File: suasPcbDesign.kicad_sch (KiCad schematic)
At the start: 94 parts, among them J1 SENSE_IB, J2 SPI CS, J4 SPI CTRL, J5 PWM CTRL, J6 JTAG Pinout, J7 USB_C_Receptacle_USB2.0_16P, SW1 SW_SPST, SW2 SW_SPST, SW3 SW_SPST, SW4 SW_SPST, SW5 SW_SPST, SW6 SW_SPST, SW7 SW_SPST, U1 74HC138, U2 LMR51625DDC, U3 MCP3562RT-E/ST, U5 TLV77733PDBVR, U6 LMV331, U7 ESP32-S3-WROOM-1, U8 LM66100DCK, U9 USBLC6-2SC6

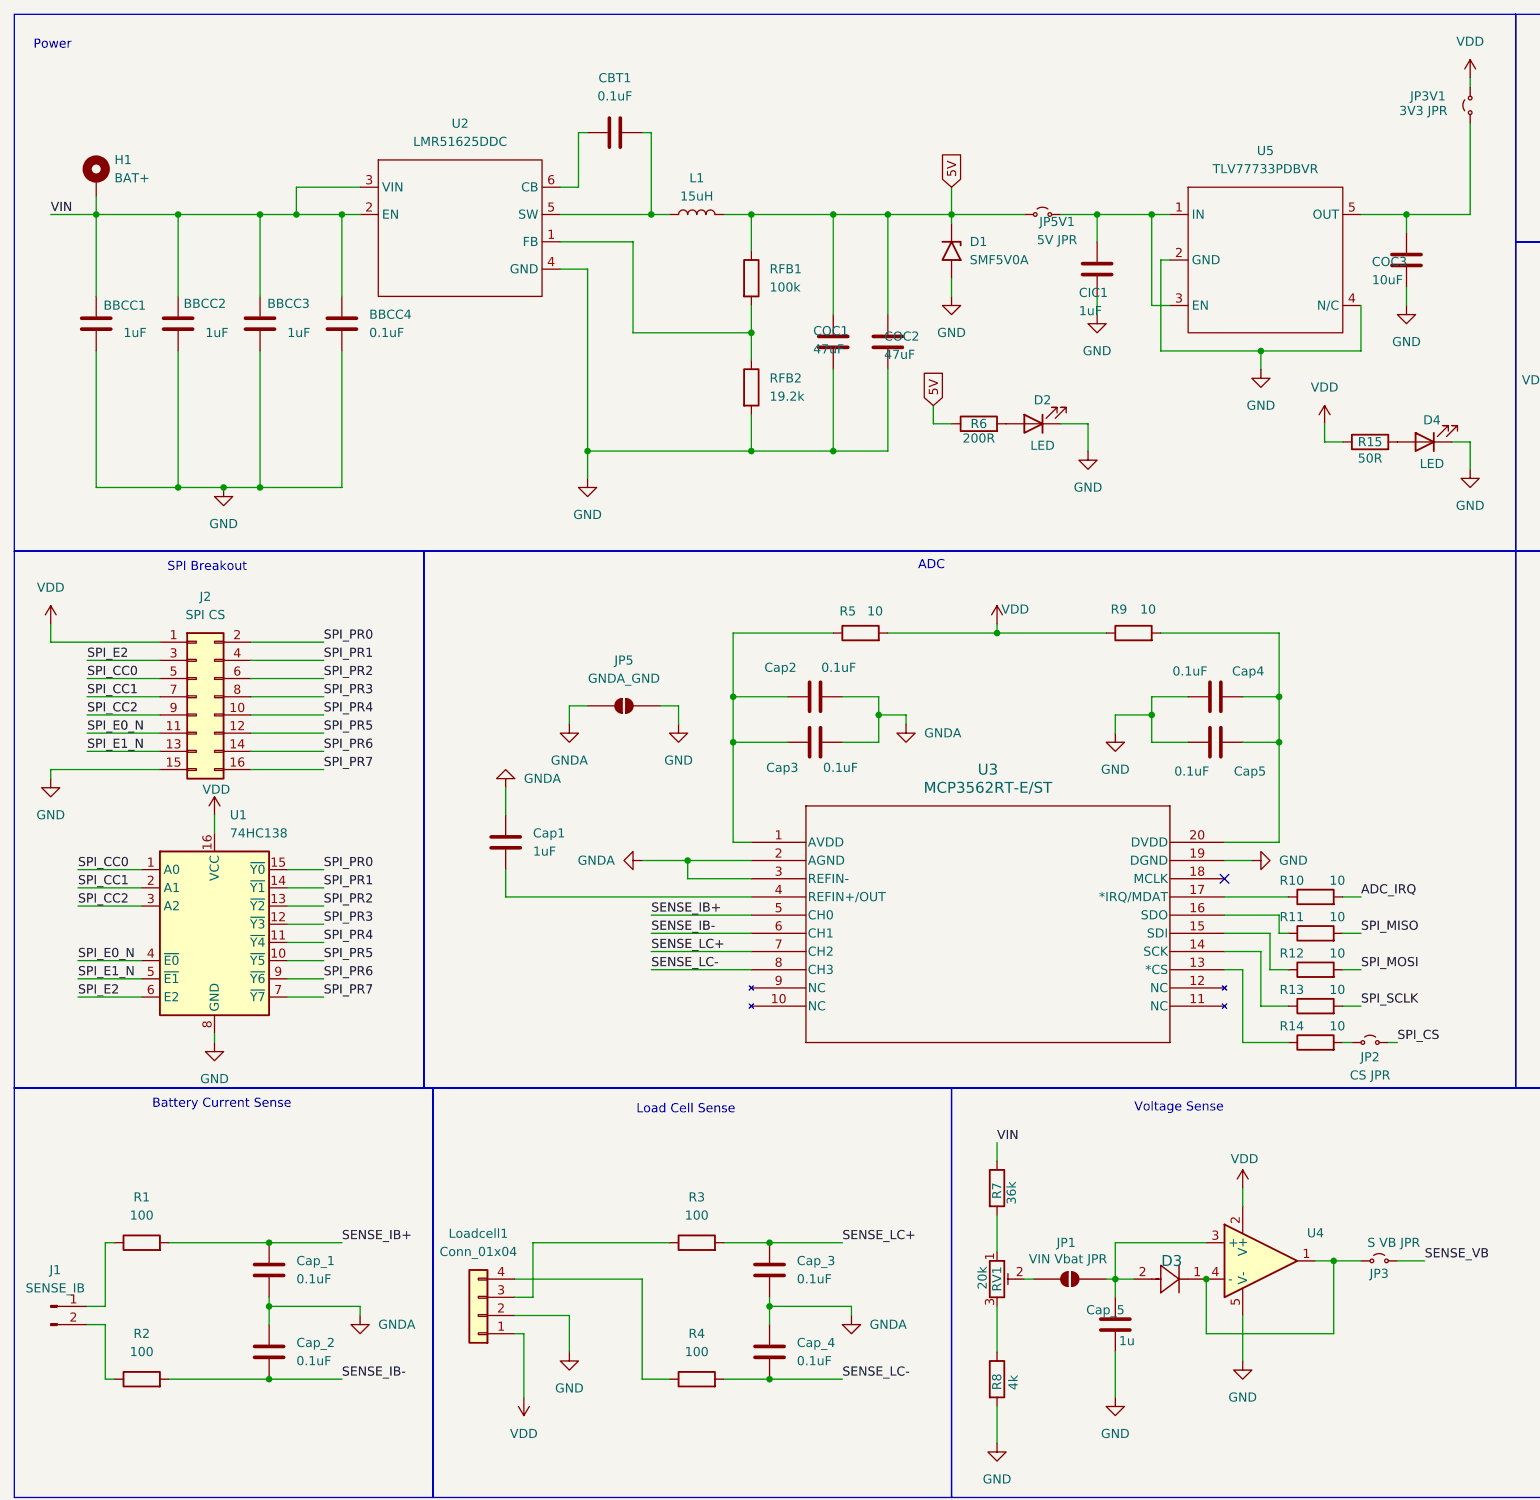
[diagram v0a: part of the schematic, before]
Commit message: Change resistor value to 100R instead of 50
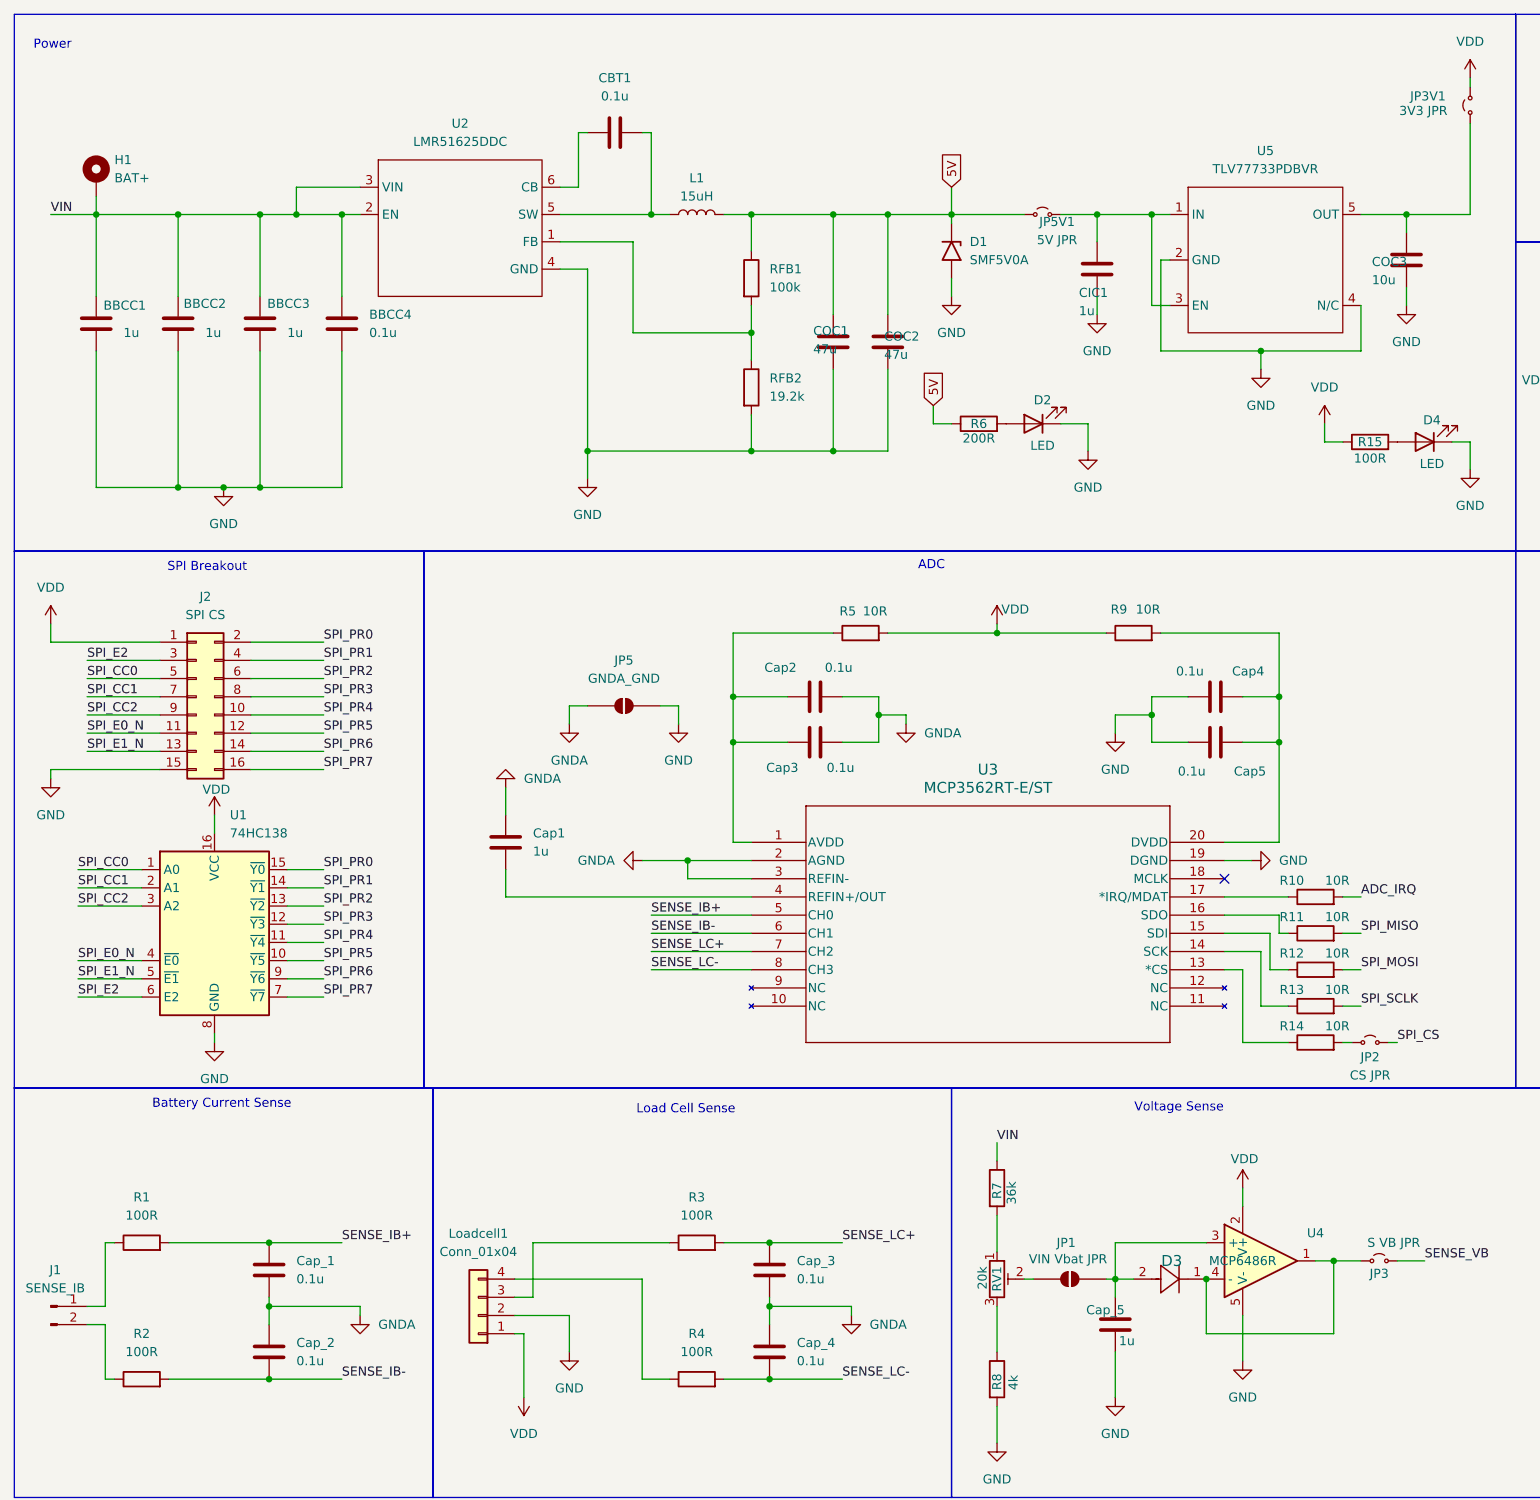
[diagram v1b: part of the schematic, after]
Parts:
- BBCC1, BBCC2, BBCC3, CIC1, Cap1: value 1uF -> 1u
- BBCC4, CBT1, Cap2, Cap3, Cap4, Cap5, Cap_1, Cap_2, Cap_3, Cap_4: value 0.1uF -> 0.1u
- COC1, COC2: value 47uF -> 47u
- COC3: value 10uF -> 10u
- R1, R2, R3, R4: value 100 -> 100R
- R10, R11, R12, R13, R14, R5, R9: value 10 -> 10R
- R15: value 50R -> 100R
- U4: value (none) -> MCP6486R
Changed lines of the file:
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@@
 			)
 		)
-		(property "Value" "47uF"
+		(property "Value" "47u"
 			(at 137.922 64.008 0)
 			(show_name no)
@@
 			)
 		)
-		(property "Value" "47uF"
+		(property "Value" "47u"
 			(at 128.016 63.246 0)
 			(show_name no)
@@
 			)
 		)
-		(property "Value" "0.1uF"
+		(property "Value" "0.1u"
 			(at 131.826 121.666 90)
 			(show_name no)
@@
 			)
 		)
-		(property "Value" "0.1uF"
+		(property "Value" "0.1u"
 			(at 180.594 108.204 90)
 			(show_name no)
@@
 			)
 		)
-		(property "Value" "1uF"
+		(property "Value" "1u"
 			(at 54.61 60.9599 0)
 			(show_name no)
@@
 			)
 		)
-		(property "Value" "50R"
+		(property "Value" "100R"
 			(at 205.74 78.486 90)
 			(show_name no)
@@
 			)
 		)
-		(property "Value" "0.1uF"
+		(property "Value" "0.1u"
 			(at 125.73 193.0399 0)
 			(show_name no)
@@
 			)
 		)
-		(property "Value" "0.1uF"
+		(property "Value" "0.1u"
 			(at 180.848 122.174 90)
 			(show_name no)
@@
 			)
 		)
-		(property "Value" "10"
+		(property "Value" "10R"
 			(at 201.168 152.654 90)
 			(show_name no)
@@
 			)
 		)
-		(property "Value" "0.1uF"
+		(property "Value" "0.1u"
 			(at 55.88 204.4699 0)
 			(show_name no)
@@
 			)
 		)
-		(property "Value" "10"
+		(property "Value" "10R"
 			(at 201.168 137.414 90)
 			(show_name no)
@@
 			)
 		)
-		(property "Value" "0.1uF"
+		(property "Value" "0.1u"
 			(at 55.88 193.0399 0)
 			(show_name no)
@@
 			)
 		)
-		(property "Value" "100"
+		(property "Value" "100R"
 			(at 111.76 184.15 90)
 			(show_name no)
@@
 			)
 		)
-		(property "Value" "10uF"
+		(property "Value" "10u"
 			(at 205.994 53.594 0)
 			(show_name no)
@@
 			)
 		)
-		(property "Value" "1uF"
+		(property "Value" "1u"
 			(at 88.9 133.3499 0)
 			(show_name no)
@@
 			)
 		)
-		(property "Value" "0.1uF"
+		(property "Value" "0.1u"
 			(at 100.33 27.94 90)
 			(show_name no)
@@
 			)
 		)
-		(property "Value" "100"
+		(property "Value" "100R"
 			(at 34.29 203.2 90)
 			(show_name no)
@@
 			)
 		)
-		(property "Value" "10"
+		(property "Value" "10R"
 			(at 201.168 147.574 90)
 			(show_name no)
@@
 			)
 		)
-		(property "Value" "100"
+		(property "Value" "100R"
 			(at 34.29 184.15 90)
 			(show_name no)
@@
 			)
 		)
-		(property "Value" "1uF"
+		(property "Value" "1u"
 			(at 31.75 60.9599 0)
 			(show_name no)
@@
 			)
 		)
-		(property "Value" "10"
+		(property "Value" "10R"
 			(at 174.752 99.568 90)
 			(show_name no)
@@
 			)
 		)
-		(property "Value" "10"
+		(property "Value" "10R"
 			(at 136.652 99.822 90)
 			(show_name no)
@@
 			)
 		)
-		(property "Value" "100"
+		(property "Value" "100R"
 			(at 111.76 203.2 90)
 			(show_name no)
@@
 			)
 		)
-		(property "Value" "1uF"
+		(property "Value" "1u"
 			(at 165.1 57.912 0)
 			(show_name no)
@@
 			)
 		)
-		(property "Value" "0.1uF"
+		(property "Value" "0.1u"
 			(at 125.73 204.4699 0)
 			(show_name no)
@@
 			)
 		)
-		(property "Value" "0.1uF"
+		(property "Value" "0.1u"
 			(at 131.572 107.696 90)
 			(show_name no)
@@
 			)
 		)
-		(property "Value" "10"
+		(property "Value" "10R"
 			(at 201.168 142.494 90)
 			(show_name no)
@@
 			)
 		)
-		(property "Value" "0.1uF"
+		(property "Value" "0.1u"
 			(at 66.04 60.9599 0)
 			(show_name no)
@@
 			)
 		)
-		(property "Value" "10"
+		(property "Value" "10R"
 			(at 201.168 157.734 90)
 			(show_name no)
@@
 			)
 		)
-		(property "Value" ""
+		(property "Value" "MCP6486R"
 			(at 187.96 190.5 0)
 			(show_name no)
@@
 			)
 		)
-		(property "Value" "1uF"
+		(property "Value" "1u"
 			(at 43.18 60.9599 0)
 			(show_name no)

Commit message: Add reverse polarity diode and edit resistor vals
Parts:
- added D9: D, Diode_SMD:D_SMA-SMB_Universal_Handsoldering, symbol Device:D
- D8: footprint Diode_SMD:D_MiniMELF_Handsoldering -> Diode_SMD:D_SMA-SMB_Universal_Handsoldering
- R15: value 100R -> 200R
- R17, R18: value 62R -> 150R
- R19: value 110R -> 75R
- R6: value 200R -> 300R
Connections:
- net IND_B: now also R19.1; no longer R17.1
- net IND_R: now also R17.1; no longer R19.1
- net VIN: now also D9.2 (A); no longer BBCC1.1, BBCC2.1, BBCC3.1, BBCC4.1, U2.2 (EN), U2.3 (VIN)
- new net: BBCC1.1, BBCC2.1, BBCC3.1, BBCC4.1, D9.1 (K), U2.2 (EN), U2.3 (VIN)
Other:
- moved on the sheet: BBCC1, BBCC2, BBCC3

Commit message: Add new comparator
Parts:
- R25: value 200R -> 300R
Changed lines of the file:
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@@
 			)
 		)
-		(property "Datasheet" "http://www.ti.com/lit/ds/symlink/lmv331.pdf"
+		(property "Datasheet" "https://ww1.microchip.com/downloads/aemDocuments/documents/MSLD/ProductDocuments/DataSheets/MCP6541-Output-Sub-Microamp-Comparators-DS20001696.pdf"
 			(at 254 63.5 0)
 			(hide yes)
@@
 			)
 		)
-		(property "Description" "Single General-Purpose Low-Voltage Comparator, SOT-23-5/SC-70-5"
+		(property "Description" "Single General-Purpose Low-Voltage Comparator, SOT-23-5/SC-70-5 (MCP6541UT-E/OTCT-ND)"
 			(at 254 68.58 0)
 			(hide yes)
@@
 			)
 		)
-		(property "Value" "200R"
+		(property "Value" "300R"
 			(at 346.71 36.576 90)
 			(show_name no)

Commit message: Update part value for comparator
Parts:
- U6: value LMV331 -> MCP6541UT-E/OT
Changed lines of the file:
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@@
 			)
 		)
-		(property "Value" "LMV331"
+		(property "Value" "MCP6541UT-E/OT"
 			(at 264.16 64.6998 0)
 			(show_name no)

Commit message: Fix diode position
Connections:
- net VIN: now also BBCC1.1, BBCC2.1, BBCC3.1, BBCC4.1, D9.1 (K), U2.2 (EN), U2.3 (VIN); no longer D9.2 (A), H1.1
- new net: D9.2 (A), H1.1
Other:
- moved on the sheet: D9, H1
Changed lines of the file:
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@@
 	)
 	(junction
+		(at 27.94 44.45)
+		(diameter 0)
+		(color 0 0 0 0)
+	)
+	(junction
 		(at 52.07 196.85)
 		(diameter 0)
@@
 	)
 	(junction
-		(at 27.94 44.45)
-		(diameter 0)
-		(color 0 0 0 0)
-	)
-	(junction
 		(at 153.67 102.87)
 		(diameter 0)
@@
 	(wire
 		(pts
-			(xy 35.56 44.45) (xy 36.83 44.45)
-		)
-		(stroke
-			(width 0)
-			(type default)
-		)
-	)
-	(wire
-		(pts
 			(xy 190.5 63.5) (xy 190.5 66.04)
 		)
@@
 	(wire
 		(pts
-			(xy 27.94 41.91) (xy 27.94 44.45)
-		)
-		(stroke
-			(width 0)
-			(type default)
-		)
-	)
-	(wire
-		(pts
 			(xy 87.63 200.66) (xy 87.63 209.55)
 		)
@@
 	(wire
 		(pts
+			(xy 27.94 44.45) (xy 36.83 44.45)
+		)
+		(stroke
+			(width 0)
+			(type default)
+		)
+	)
+	(wire
+		(pts
 			(xy 276.86 186.69) (xy 276.86 187.96)
 		)
@@
 	(wire
 		(pts
+			(xy 27.94 43.18) (xy 27.94 44.45)
+		)
+		(stroke
+			(width 0)
+			(type default)
+		)
+	)
+	(wire
+		(pts
+			(xy 27.94 34.29) (xy 27.94 35.56)
+		)
+		(stroke
+			(width 0)
+			(type default)
+		)
+	)
+	(wire
+		(pts
 			(xy 245.11 71.12) (xy 245.11 73.66)
 		)
@@
 	(symbol
 		(lib_id "Device:D")
-		(at 31.75 44.45 180)
+		(at 27.94 39.37 90)
 		(unit 1)
 		(body_style 1)
@@
 		(dnp no)
 		(property "Reference" "D9"
-			(at 31.496 47.498 0)
+			(at 24.892 39.116 0)
 			(show_name no)
 			(do_not_autoplace no)
@@
 		)
 		(property "Value" "D"
-			(at 31.496 50.038 0)
+			(at 22.352 39.116 0)
 			(show_name no)
 			(do_not_autoplace no)
@@
 		)
 		(property "Footprint" "Diode_SMD:D_SMA-SMB_Universal_Handsoldering"
-			(at 31.75 44.45 0)
+			(at 27.94 39.37 0)
 			(hide yes)
 			(show_name no)
@@
 		)
 		(property "Datasheet" "https://mm.digikey.com/Volume0/opasdata/d220001/medias/docus/6956/5399_S3M%20SMB.pdf"
-			(at 31.75 44.45 0)
+			(at 27.94 39.37 0)
 			(hide yes)
 			(show_name no)
@@
 		)
 		(property "Description" "Diode 5399-S3MCT-ND"
-			(at 31.75 44.45 0)
+			(at 27.94 39.37 0)
 			(hide yes)
 			(show_name no)
@@
 		)
 		(property "Sim.Device" "D"
-			(at 31.75 44.45 0)
+			(at 27.94 39.37 0)
 			(hide yes)
 			(show_name no)
@@
 		)
 		(property "Sim.Pins" "1=K 2=A"
-			(at 31.75 44.45 0)
+			(at 27.94 39.37 0)
 			(hide yes)
 			(show_name no)
@@
 	(symbol
 		(lib_id "Mechanical:MountingHole_Pad")
-		(at 27.94 39.37 0)
+		(at 27.94 31.75 0)
 		(unit 1)
 		(body_style 1)
@@
 		(fields_autoplaced yes)
 		(property "Reference" "H1"
-			(at 30.48 36.8299 0)
+			(at 30.48 29.2099 0)
 			(show_name no)
 			(do_not_autoplace no)
@@
 		)
 		(property "Value" "BAT+"
-			(at 30.48 39.3699 0)
+			(at 30.48 31.7499 0)
 			(show_name no)
 			(do_not_autoplace no)
@@
 		)
 		(property "Footprint" "Custom:7770 Keystone Electronics PC SCREW TERMINALS"
-			(at 27.94 39.37 0)
+			(at 27.94 31.75 0)
 			(hide yes)
 			(show_name no)
@@
 		)
 		(property "Datasheet" ""
-			(at 27.94 39.37 0)
+			(at 27.94 31.75 0)
 			(hide yes)
 			(show_name no)
@@
 		)
 		(property "Description" "Mounting Hole with connection"
-			(at 27.94 39.37 0)
+			(at 27.94 31.75 0)
 			(hide yes)
 			(show_name no)

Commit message: Include battery terminal in BOM
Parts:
- H1: now in the parts list
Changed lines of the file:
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@@
 		(body_style 1)
 		(exclude_from_sim no)
-		(in_bom no)
+		(in_bom yes)
 		(on_board yes)
 		(in_pos_files yes)
@@
 			)
 		)
-		(property "Datasheet" ""
+		(property "Datasheet" "https://www.keyelco.com/userAssets/file/K75p76.pdf"
 			(at 27.94 31.75 0)
 			(hide yes)
